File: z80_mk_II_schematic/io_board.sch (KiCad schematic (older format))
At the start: 2 parts

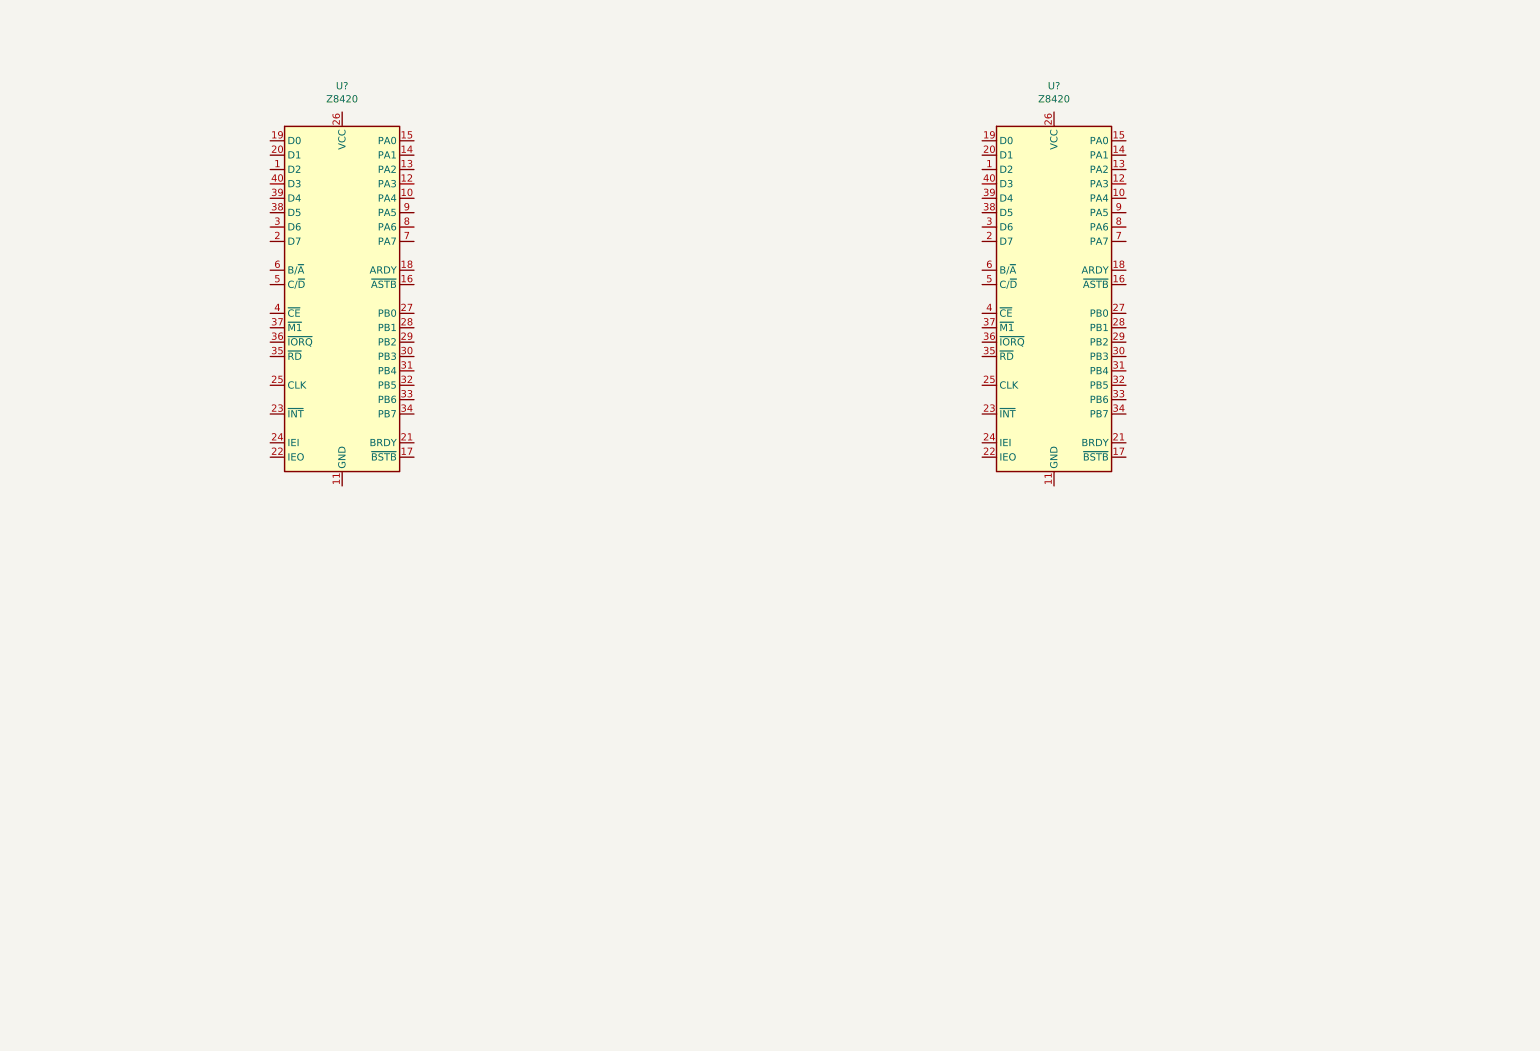
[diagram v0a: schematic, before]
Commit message: UART section of IO board completed.
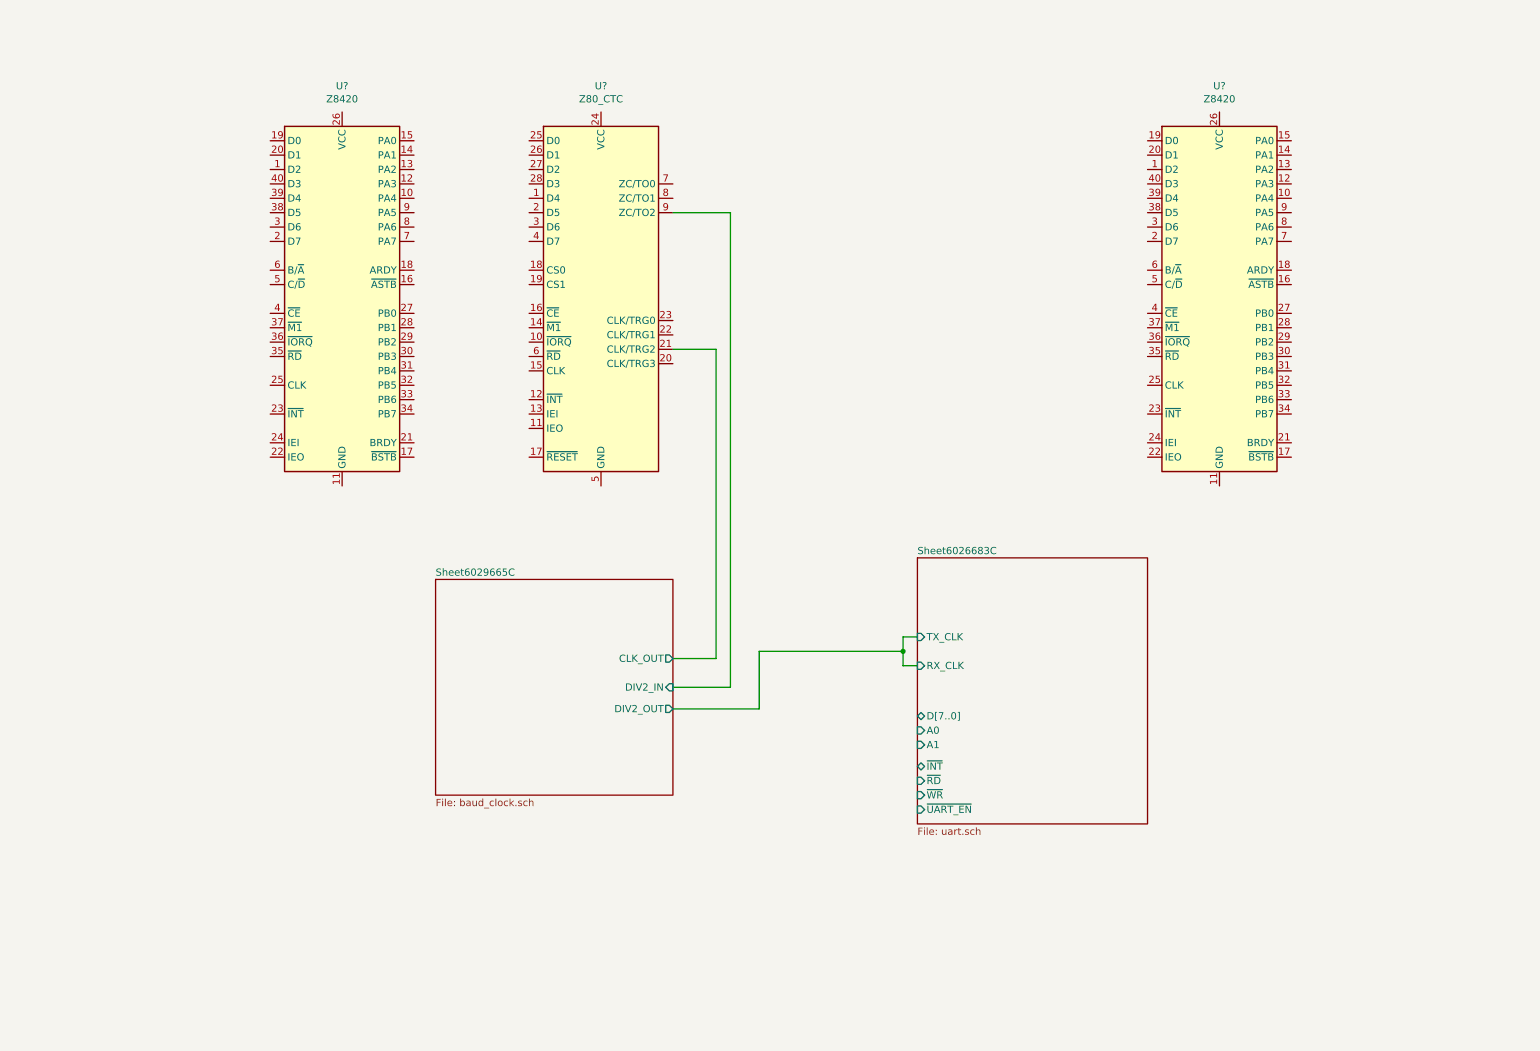
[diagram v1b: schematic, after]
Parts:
- added U?: Z80_CTC, Housings_DIP:DIP-28_W15.24mm, symbol jm_Z80:Z80_CTC
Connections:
- new net Sheet6029665C/CLK_OUT: U?.21 (CLK/TRG2)
- new net Sheet6029665C/DIV2_IN: U?.9 (ZC/TO2)
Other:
- moved on the sheet: U?
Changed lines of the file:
@@
 $Descr A4 11693 8268
 encoding utf-8
-Sheet 3 4
+Sheet 3 6
 Title ""
 Date ""
@@
 L Interface:Z8420 U?
 U 1 1 5FC1756B
-P 7800 2550
-F 0 "U?" H 7800 4031 50  0000 C CNN
-F 1 "Z8420" H 7800 3940 50  0000 C CNN
-F 2 "Package_DIP:DIP-40_W15.24mm" H 7800 1150 50  0001 C CNN
-F 3 "https://www.zilog.com/appnotes_download.php?FromPage=DirectLink&dn=PS0180&ft=Product%20Specification%20(Data%20Sheet)%20%20&f=YUhSMGNEb3ZMM2QzZHk1NmFXeHZaeTVqYjIwdlpHOWpjeTk2T0RBdmNITXdNVGd3TG5Ca1pnPT0=" H 7750 950 50  0001 C CNN
-	1    7800 2550
+P 8950 2550
+F 0 "U?" H 8950 4031 50  0000 C CNN
+F 1 "Z8420" H 8950 3940 50  0000 C CNN
+F 2 "Package_DIP:DIP-40_W15.24mm" H 8950 1150 50  0001 C CNN
+F 3 "https://www.zilog.com/appnotes_download.php?FromPage=DirectLink&dn=PS0180&ft=Product%20Specification%20(Data%20Sheet)%20%20&f=YUhSMGNEb3ZMM2QzZHk1NmFXeHZaeTVqYjIwdlpHOWpjeTk2T0RBdmNITXdNVGd3TG5Ca1pnPT0=" H 8900 950 50  0001 C CNN
+	1    8950 2550
 	1    0    0    -1
 $EndComp
+$Comp
+L jm_Z80:Z80_CTC U?
+U 1 1 60257463
+P 4650 2550
+F 0 "U?" H 4650 4031 50  0000 C CNN
+F 1 "Z80_CTC" H 4650 3940 50  0000 C CNN
+F 2 "Housings_DIP:DIP-28_W15.24mm" H 4650 1150 50  0001 C CNN
+F 3 "https://www.zilog.com/docs/z80/um0081.pdf" H 4600 950 50  0001 C CNN
+	1    4650 2550
+	1    0    0    -1
+$EndComp
+$Sheet
+S 3500 4500 1650 1500
+U 6029665D
+F0 "Sheet6029665C" 50
+F1 "baud_clock.sch" 50
+F2 "CLK_OUT" O R 5150 5050 50
+F3 "DIV2_OUT" O R 5150 5400 50
+F4 "DIV2_IN" I R 5150 5250 50
+$EndSheet
+Wire Wire Line
+	5150 1950 5550 1950
+Wire Wire Line
+	5550 1950 5550 5250
+Wire Wire Line
+	5550 5250 5150 5250
+Wire Wire Line
+	5450 2900 5150 2900
+Wire Wire Line
+	5450 5050 5450 2900
+Wire Wire Line
+	5150 5050 5450 5050
+$Sheet
+S 6850 4350 1600 1850
+U 6026683D
+F0 "Sheet6026683C" 50
+F1 "uart.sch" 50
+F2 "TX_CLK" I L 6850 4900 50
+F3 "RX_CLK" I L 6850 5100 50
+F4 "D[7..0]" B L 6850 5450 50
+F5 "~INT~" T L 6850 5800 50
+F6 "~RD~" I L 6850 5900 50
+F7 "~UART_EN~" I L 6850 6100 50
+F8 "~WR~" I L 6850 6000 50
+F9 "A0" I L 6850 5550 50
+F10 "A1" I L 6850 5650 50
+$EndSheet
+Wire Wire Line
+	5150 5400 5750 5400
+Wire Wire Line
+	5750 5400 5750 5000
+Wire Wire Line
+	5750 5000 6750 5000
+Wire Wire Line
+	6750 5000 6750 5100
+Wire Wire Line
+	6750 5100 6850 5100
+Wire Wire Line
+	6850 4900 6750 4900
+Wire Wire Line
+	6750 4900 6750 5000
+Connection ~ 6750 5000
 $EndSCHEMATC

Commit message: Lots more work on schematic
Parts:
- added C19, C20, C21: 0u1, symbol Device:C_Small
- added D11, D12, D13, D14, D15, D16, D17, D18, D19, D20: 1N4148, Diode_THT:D_DO-35_SOD27_P7.62mm_Horizontal, symbol Diode:1N4148
- added J2, J4: Conn_02x10_Odd_Even, symbol Connector_Generic:Conn_02x10_Odd_Even
- added J3: Conn_02x08_Odd_Even, symbol Connector_Generic:Conn_02x08_Odd_Even
- added U12: 74LS00, symbol 74xx:74LS00
- added U14, U16: 74LS245, symbol 74xx:74LS245
- added U15: 74LS145, symbol 74xx:74LS145
- added U18: 74LS138, symbol 74xx:74LS138
- U13, U19: renamed from U?; value Z8420 -> Z80_PIO; footprint Package_DIP:DIP-40_W15.24mm -> (none)
- U17: renamed from U?; footprint Housings_DIP:DIP-28_W15.24mm -> (none)
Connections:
- net DB2: now reaches U13.1 (D2)
- net DB2: now also U17.27 (D2), U19.1 (D2), J3.4 (Pin_4), U14.13 (B5)
- net at U13.10 (PA4): now also D11.1 (K), D12.1 (K), D13.1 (K), D14.1 (K), D15.1 (K), D16.1 (K), D17.1 (K), D18.1 (K), D19.1 (K), D20.1 (K)
- net GND: now reaches U13.11 (GND)
- net GND: now also U17.5 (GND), U19.11 (GND), C19.2, C20.2, C21.2, J2.12 (Pin_12), J3.16 (Pin_16), J4.19 (Pin_19), U12.7 (GND), U14.10 (GND), U14.19 (CE), U16.10 (GND), U16.19 (CE), U18.8 (GND)
- net at U13.12 (PA3): now also U15.12 (P3)
- net at U13.13 (PA2): now also U15.13 (P2)
- net at U13.14 (PA1): now also U15.14 (P1)
- net at U13.15 (PA0): now also U15.15 (P0)
- net DB0: now reaches U13.19 (D0)
- net DB0: now also U17.25 (D0), U19.19 (D0), J3.2 (Pin_2), U14.11 (B7)
- net DB7: now reaches U13.2 (D7)
- net DB7: now also U17.4 (D7), U19.2 (D7), J3.9 (Pin_9), U14.18 (B0)
- net DB1: now reaches U13.20 (D1)
- net DB1: now also U17.26 (D1), U19.20 (D1), J3.3 (Pin_3), U14.12 (B6)
- net at U13.22 (IEO): now also U17.13 (IEI)
- net ~INT~: now reaches U13.23 (~INT~)
- net ~INT~: now also U17.12 (~INT~), U19.23 (~INT~)
- net +5V: now reaches U13.24 (IEI)
- net +5V: now also U13.26 (VCC), U17.24 (VCC), U19.26 (VCC), C19.1, C20.1, C21.1, J3.1 (Pin_1), U12.14 (VCC), U14.20 (VCC), U15.16 (VCC), U16.1 (A->B), U16.20 (VCC), U18.16 (VCC), U18.6 (E3)
- net ~IOCLK~: now reaches U13.25 (CLK)
- net ~IOCLK~: now also U17.15 (CLK), U19.25 (CLK), J3.13 (Pin_13)
- net at U13.27 (PB0): now also J2.13 (Pin_13)
- net at U13.28 (PB1): now also J2.14 (Pin_14)
- net at U13.29 (PB2): now also J2.15 (Pin_15)
- net DB6: now reaches U13.3 (D6)
- net DB6: now also U17.3 (D6), U19.3 (D6), J3.8 (Pin_8), U14.17 (B1)
- net at U13.30 (PB3): now also J2.16 (Pin_16)
- net at U13.31 (PB4): now also J2.17 (Pin_17)
- net at U13.32 (PB5): now also J2.18 (Pin_18)
- net at U13.33 (PB6): now also J2.19 (Pin_19)
- net at U13.34 (PB7): now also J2.20 (Pin_20)
- net ~RD~: now reaches U13.35 (~RD~)
- net ~RD~: now also U17.6 (~RD~), U19.35 (~RD~), J3.11 (Pin_11), U12.12
- net ~IORQ~: now reaches U13.36 (~IORQ~)
- net ~IORQ~: now also U17.10 (~IORQ~), U19.36 (~IORQ~), U12.10, U12.9, U18.5 (E2)
- net ~M1~: now reaches U13.37 (~M1~)
- net ~M1~: now also U17.14 (~M1~), U19.37 (~M1~), U12.13
- net DB5: now reaches U13.38 (D5)
- net DB5: now also U17.2 (D5), U19.38 (D5), J3.7 (Pin_7), U14.16 (B2)
- net DB4: now reaches U13.39 (D4)
- net DB4: now also U17.1 (D4), U19.39 (D4), J3.6 (Pin_6), U14.15 (B3)
- net ~PIO1_CE~: now reaches U13.4 (~CE~)
- net ~PIO1_CE~: now also U18.15 (O0)
- net DB3: now reaches U13.40 (D3)
- net DB3: now also U17.28 (D3), U19.40 (D3), J3.5 (Pin_5), U14.14 (B4)
- net AB1: now reaches U13.5 (C/~D~)
- net AB1: now also U17.19 (CS1), U19.5 (C/~D~), U16.12 (B6)
- net AB0: now reaches U13.6 (B/~A~)
- net AB0: now also U17.18 (CS0), U19.6 (B/~A~), J3.10 (Pin_10), U16.11 (B7)
- net at U19.10 (PA4): now also J4.14 (Pin_14)
- net at U19.12 (PA3): now also J4.12 (Pin_12)
- net at U19.13 (PA2): now also J4.10 (Pin_10)
- net at U19.14 (PA1): now also J4.8 (Pin_8)
- net at U19.15 (PA0): now also J4.6 (Pin_6)
- net at U19.16 (~ASTB~): now also J4.4 (Pin_4)
- net at U19.18 (ARDY): now also J4.2 (Pin_2)
- net at U19.24 (IEI): now also U17.11 (IEO)
- net ~PIO2_CE~: now reaches U19.4 (~CE~)
- net ~PIO2_CE~: now also U18.11 (O4)
- net at U19.7 (PA7): now also J4.20 (Pin_20)
- net at U19.8 (PA6): now also J4.18 (Pin_18)
- net at U19.9 (PA5): now also J4.16 (Pin_16)
- net ~CTC_CE~: now reaches U17.16 (~CE~)
- net ~CTC_CE~: now also U18.14 (O1)
- net ~RESET~: now reaches U17.17 (~RESET~)
- net ~RESET~: now also J3.15 (Pin_15)
- new net: D11.2 (A), J2.1 (Pin_1), U15.1 (Q0)
- new net: D20.2 (A), J2.10 (Pin_10), U15.11 (Q9)
- new net: D12.2 (A), J2.2 (Pin_2), U15.2 (Q1)
- new net: D13.2 (A), J2.3 (Pin_3), U15.3 (Q2)
- new net: D14.2 (A), J2.4 (Pin_4), U15.4 (Q3)
- new net: D15.2 (A), J2.5 (Pin_5), U15.5 (Q4)
- new net: D16.2 (A), J2.6 (Pin_6), U15.6 (Q5)
- new net: D17.2 (A), J2.7 (Pin_7), U15.7 (Q6)
- new net: D18.2 (A), J2.8 (Pin_8), U15.9 (Q7)
- new net: D19.2 (A), J2.9 (Pin_9), U15.10 (Q8)
- new net: U12.6, U14.1 (A->B)
- new net: U12.5, U12.8
- new net: U12.11, U12.4
- new net A0: U16.9 (A7)
- new net A1: U16.8 (A6)
- new net A2: U16.7 (A5)
- new net A3: U16.6 (A4)
- new net A4: U16.5 (A3)
- new net A5: U16.4 (A2)
- new net A6: U16.3 (A1)
- new net A7: U16.2 (A0)
- new net AB2: U16.13 (B5)
- new net AB3: U16.14 (B4)
- new net AB4: U16.15 (B3), U18.1 (A0)
- new net AB5: U16.16 (B2), U18.2 (A1)
- new net AB6: U16.17 (B1), U18.3 (A2)
- new net AB7: U16.18 (B0), U18.4 (E1)
- new net D0: U14.9 (A7)
- new net D1: U14.8 (A6)
- new net D2: U14.7 (A5)
- new net D3: U14.6 (A4)
- new net D4: U14.5 (A3)
- new net D5: U14.4 (A2)
- new net D6: U14.3 (A1)
- new net D7: U14.2 (A0)
- new net ~LCD_CE~: J3.14 (Pin_14), U18.12 (O3)
- new net ~UART_CE~: U18.13 (O2)
- new net ~WR~: J3.12 (Pin_12)
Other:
- note added: "KEYBOARD"
- note added: "LCD"
- note added: "Possible open-circuit\nat IEI on CTC socket"
- note added: "This wire is currently not joined\ntogether."
- note added: "USER PORT"
- moved on the sheet: U13, U17, U19
